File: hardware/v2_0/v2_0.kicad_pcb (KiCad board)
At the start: 2 copper layers, 90 parts, among them J1 USB_B_Mini, J11 NRFSWDCLK, J12 NRFSWDIO, J13 GND, J14 NRFGPIO, J15 USB_B_Mini, J16 DRV1_MTR2, J18 USB_A, J19 Conn_01x02_Male, J2 CAN, J3 PWR, J4 Power_terminal, J5 DRV1_MTR1, J6 DRV1_MTR2, J7 Conn_01x02_Male, J8 DRV1_MTR1, J9 UART, P1 SWD, Q1 Q_NMOS_GSD, Q2 Q_NMOS_GSD, U1 TJA1051TK-3, U10 DRV8848, U2 STM32F40X_LQFP64, U3 BMI160, U4 MCP16311/2, U5 DRV8848, U8 BMD-340-A-R, U9 ADP2303ARDZ-5.0, Y1 8M

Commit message: I hope it is time for routing soon
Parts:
- added J10: SERV1, Connector_PinHeader_2.54mm:PinHeader_1x03_P2.54mm_Vertical, F.Cu at (142.5, 71.0)
- added P2: SWD, Connector_JST:JST_PH_B6B-PH-K_1x06_P2.00mm_Vertical, F.Cu at (171.0, 104.3)
- added R19: 220R, Resistor_SMD:R_0603_1608Metric, F.Cu at (132.7, 96.0)
- added R20: 220R, Resistor_SMD:R_0603_1608Metric, F.Cu at (145.3, 82.2)
- added R21: 22R, Resistor_SMD:R_0603_1608Metric_Pad1.05x0.95mm_HandSolder, F.Cu at (150.2, 121.5)
- added R22: 22R, Resistor_SMD:R_0603_1608Metric_Pad1.05x0.95mm_HandSolder, F.Cu at (154.6, 121.5)
- J11: value NRFSWDCLK -> SERV2; footprint TestPoint:TestPoint_Pad_1.5x1.5mm -> Connector_PinHeader_2.54mm:PinHeader_1x03_P2.54mm_Vertical
- J12: value NRFSWDIO -> SPI; footprint TestPoint:TestPoint_Pad_1.5x1.5mm -> Connector_JST:JST_PH_B6B-PH-K_1x06_P2.00mm_Vertical
- J13: value GND -> UART5; footprint TestPoint:TestPoint_Pad_1.5x1.5mm -> Connector_JST:JST_PH_B4B-PH-K_1x04_P2.00mm_Vertical
- J9: value UART -> USART4_UART4
- moved J12 68.4 mm to (100.8, 78.0)
- moved C23 53.4 mm to (130.0, 120.9)
- moved R8 49.6 mm to (103.8, 126.8)
- moved R6 48.9 mm to (99.8, 126.8)
- moved R2 48.8 mm to (146.8, 75.0)
- moved C17 48.1 mm to (122.7, 125.4)
- moved R12 46.9 mm to (134.0, 120.1)
- moved C7 44.8 mm to (146.8, 72.5)
- moved R5 43.8 mm to (144.7, 84.7)
- moved U2 43.0 mm to (121.0, 76.0)
- moved R10 42.0 mm to (196.1, 74.5)
- moved C19 41.4 mm to (142.9, 110.7)
- moved J13 41.2 mm to (125.7, 85.9)
- moved C21 41.1 mm to (130.0, 118.3)
- moved R3 40.9 mm to (140.8, 88.7)
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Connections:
- net Net-(U2-Pad53) renamed /base_sheet/UART5_TX
- net Net-(U2-Pad54) renamed /base_sheet/UART5_RX
- J11 pad 1: NRFSWDCLK -> Net-(J11-Pad1)
- J12 pad 1: NRFSWDIO -> /base_sheet/SPI2_MOSI
- J15 pad 2: NRFUSBD- -> Net-(J15-Pad2)
- J15 pad 3: NRFUSBD+ -> Net-(J15-Pad3)
- U2 pad 10: Net-(U2-Pad10) -> NRFSWDCLK
- U2 pad 29: Net-(U2-Pad29) -> /base_sheet/SERV1
- U2 pad 30: Net-(U2-Pad30) -> /base_sheet/SERV2
- U2 pad 33: Net-(U2-Pad33) -> /base_sheet/SPI2_NSS
- U2 pad 34: Net-(U2-Pad34) -> /base_sheet/SPI2_SCK
- U2 pad 35: NRFSWDIO -> /base_sheet/SPI2_MISO
- U2 pad 36: NRFSWDCLK -> /base_sheet/SPI2_MOSI
- U2 pad 9: Net-(U2-Pad9) -> NRFSWDIO

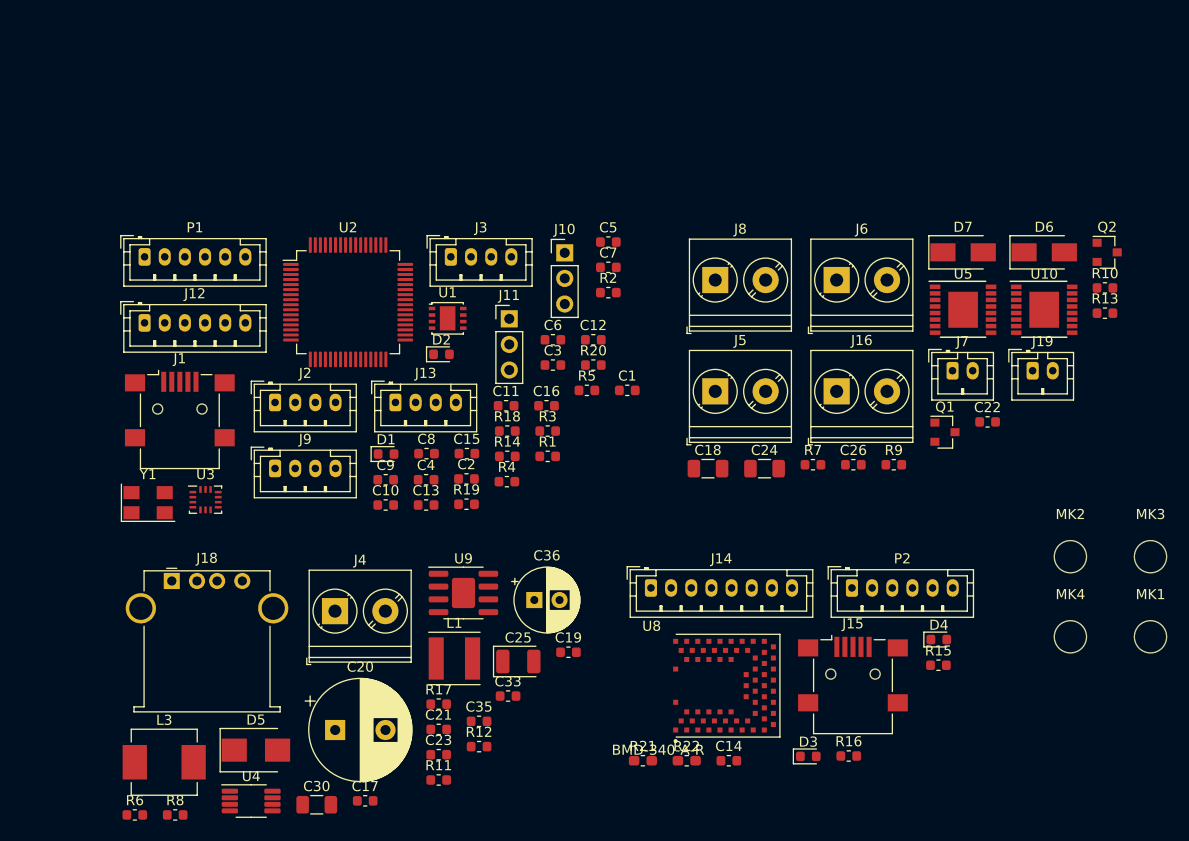
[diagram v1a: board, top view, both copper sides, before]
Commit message: adding an audio jack!
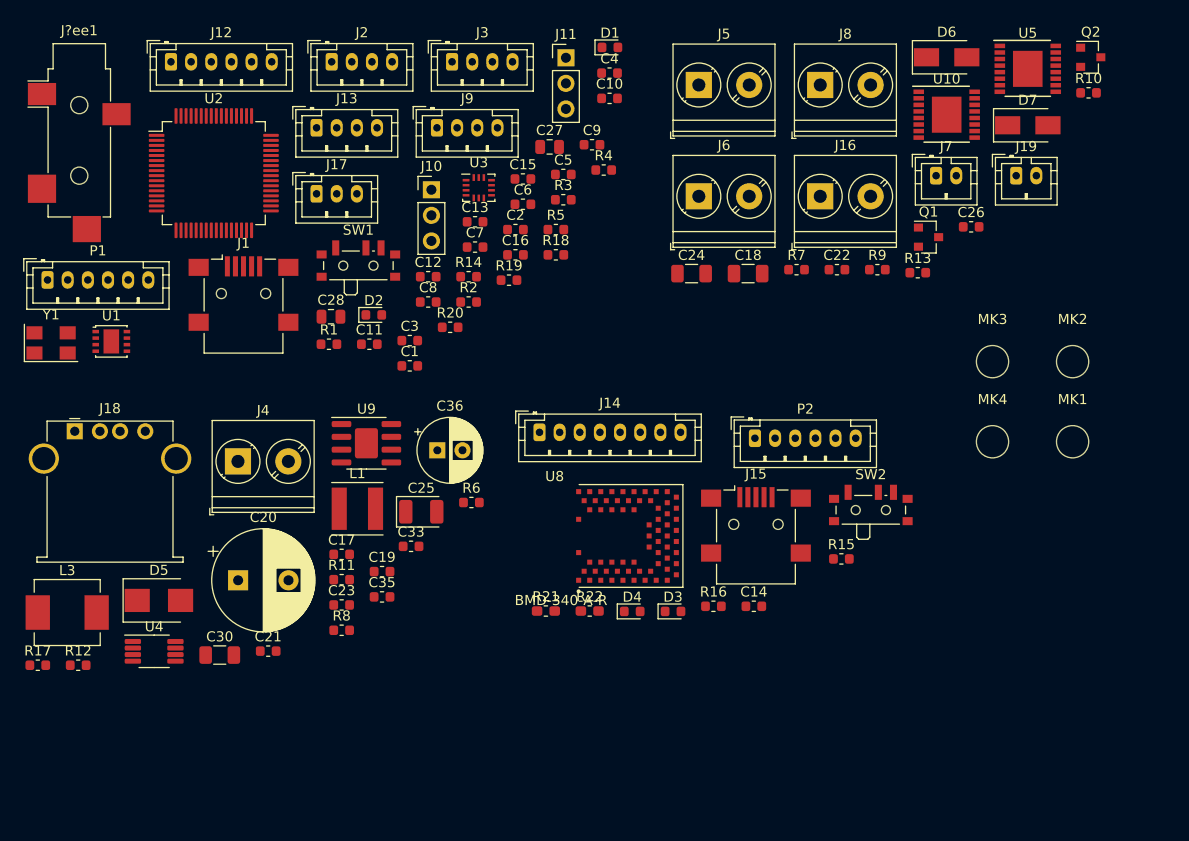
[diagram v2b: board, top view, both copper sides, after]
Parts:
- added C27: 10uF, Capacitor_SMD:C_0805_2012Metric, F.Cu at (141.0, 60.5)
- added C28: 10uF, Capacitor_SMD:C_0805_2012Metric, F.Cu at (119.3, 77.4)
- added J17: Conn_01x03_Male, Connector_JST:JST_PH_B3B-PH-K_1x03_P2.00mm_Vertical, F.Cu at (117.9, 65.2)
- added J?ee1: AudioJack3_Ground, Connector_Audio:Jack_3.5mm_CUI_SJ-3524-SMT_Horizontal, F.Cu at (94.3, 58.9)
- added SW1: MCU_USB_POWER, Button_Switch_SMD:SW_SPDT_PCM12, F.Cu at (122.0, 72.0)
- added SW2: NRF_USB_POWER, Button_Switch_SMD:SW_SPDT_PCM12, F.Cu at (172.9, 96.2)
- J19: value Conn_01x02_Male -> MTR1_CON
- J7: value Conn_01x02_Male -> MTR2_CON
- R14, R18: value R_Small -> 22R
- moved C10 46.1 mm to (146.9, 55.7)
- moved D1 46.1 mm to (147.0, 50.7)
- moved R6 45.6 mm to (133.2, 95.8)
- moved C4 44.3 mm to (146.9, 53.2)
- moved U3 41.2 mm to (134.0, 64.6)
- moved R12 40.6 mm to (94.2, 112.0)
- moved R17 40.0 mm to (90.2, 112.0)
- moved C9 39.1 mm to (145.2, 60.3)
- moved J9 37.4 mm to (129.8, 58.6)
- moved J2 34.3 mm to (119.4, 52.1)
- moved U1 33.5 mm to (97.5, 79.8)
- moved R4 32.4 mm to (146.4, 62.8)
- moved D4 30.6 mm to (149.2, 106.6)
- moved J5 30.5 mm to (155.8, 54.4)
- moved C13 28.5 mm to (133.6, 68.0)
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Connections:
- J1 pad 1: +5V -> Net-(J1-Pad1)
- J15 pad 1: +5V -> Net-(J15-Pad1)

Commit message: tweaks
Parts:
- added C29: 100uF, Capacitor_THT:CP_Radial_D10.0mm_P5.00mm, F.Cu at (114.9, 106.0)
- added C31: 100uF, Capacitor_THT:CP_Radial_D10.0mm_P5.00mm, F.Cu at (114.9, 117.5)
- added SW3: BOOT0, Button_Switch_SMD:SW_SPDT_PCM12, F.Cu at (118.9, 78.2)
- D6, D7: footprint Diode_SMD:D_SMA -> Diode_SMD:D_SMB
- J17: value Conn_01x03_Male -> DAC
- P2: value SWD -> NRFSWD
- moved D6 115.3 mm to (91.5, 125.1)
- moved R17 114.9 mm to (197.6, 71.3)
- moved R10 114.5 mm to (106.0, 127.8)
- moved Q2 111.1 mm to (111.8, 125.6)
- moved D7 110.9 mm to (99.8, 125.1)
- moved J8 98.8 mm to (90.8, 116.3)
- moved R12 94.8 mm to (184.7, 84.0)
- moved C26 88.8 mm to (116.1, 127.1)
- moved J19 85.4 mm to (126.2, 123.0)
- moved J5 82.5 mm to (90.8, 105.2)
- moved U5 79.6 mm to (127.2, 103.6)
- moved C21 78.4 mm to (184.7, 78.9)
- moved R13 77.2 mm to (120.1, 124.6)
- moved J16 76.2 mm to (102.9, 105.2)
- moved J7 75.1 mm to (126.2, 116.4)
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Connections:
- U2 pad 28: Net-(U2-Pad28) -> GND
- U2 pad 60: GND -> /base_sheet/BOOT0
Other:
- copper layers 2 -> 4
- rule pad_to_mask_clearance: 0.051 -> 0.01
- rule solder_mask_min_width: 0.25 -> 0.025
- rule trace_min: 0.2 -> 0.18
- rule via_min_size: 0.4 -> 0.3

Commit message: small tweaks
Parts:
- added C32: 47uF, Capacitor_THT:CP_Radial_D6.3mm_P2.50mm, F.Cu at (174.4, 48.1)
- J?ee1: footprint Connector_Audio:Jack_3.5mm_CUI_SJ-3524-SMT_Horizontal -> v2_0:Jack_3.5mm_CUI_SJ-3524-SMT_Horizontal
- U8: footprint crf1:RIGADO_BMD-340-A-R -> v2_0:RIGADO_BMD-340-A-R
- moved Q1 41.3 mm to (92.3, 107.6)
- moved C13 38.4 mm to (98.6, 77.2)
- moved J4 38.0 mm to (136.5, 65.3)
- moved Q2 37.9 mm to (113.9, 87.8)
- moved R7 36.8 mm to (96.5, 109.1)
- moved R13 36.7 mm to (86.4, 109.9)
- moved C36 36.5 mm to (157.7, 65.2)
- moved J16 36.4 mm to (71.2, 87.2)
- moved C26 35.8 mm to (113.7, 91.3)
- moved C31 35.4 mm to (95.4, 88.0)
- moved R12 35.2 mm to (152.7, 69.4)
- moved C20 35.0 mm to (154.9, 50.0)
- moved J6 35.0 mm to (83.3, 87.2)
- moved C8 33.8 mm to (122.3, 58.1)
- moved C7 33.3 mm to (113.1, 65.4)
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
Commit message: tweaks prepare for routing
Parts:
- moved SW2 43.0 mm to (182.2, 126.6)
- moved J?ee1 38.8 mm to (100.6, 79.3)
- moved C10 37.0 mm to (139.2, 93.9)
- moved C18 37.0 mm to (141.2, 109.5)
- moved C5 37.0 mm to (149.5, 80.8)
- moved D2 37.0 mm to (153.2, 75.7)
- moved C13 37.0 mm to (125.3, 102.8)
- moved C17 37.0 mm to (199.6, 88.3)
- moved C21 37.0 mm to (198.6, 83.3)
- moved C22 37.0 mm to (127.2, 132.2)
- moved C23 37.0 mm to (191.6, 91.1)
- moved C24 37.0 mm to (113.9, 132.6)
- moved C26 37.0 mm to (140.4, 116.9)
- moved C27 37.0 mm to (145.2, 81.0)
- moved C31 37.0 mm to (122.1, 113.6)
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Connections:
- C29 pad 1: VIN -> V_IN
- C31 pad 1: VIN -> V_IN

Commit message: fixed mistake in schematics
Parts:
- J9: value USART4_UART4 -> USART3_UART4
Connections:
- J13 pad 2: UART_RXD -> /base_sheet/UART5_RX
- J13 pad 3: UART_TXD -> /base_sheet/UART5_TX

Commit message: started routing
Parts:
- moved J3 117.1 mm to (240.2, 94.2), turned to -90 degrees
- moved J4 80.9 mm to (237.0, 57.6), turned to 90 degrees
- moved J10 71.6 mm to (206.0, 72.6), turned to 90 degrees
- moved R12 69.5 mm to (229.6, 47.0), turned to -90 degrees
- moved J18 64.7 mm to (229.0, 83.6), turned to 90 degrees
- moved C30 60.6 mm to (221.8, 57.4), turned to 90 degrees
- moved J11 57.2 mm to (206.0, 69.0), turned to 90 degrees
- moved C33 56.7 mm to (231.2, 47.0), turned to 90 degrees
- moved C14 56.1 mm to (218.0, 152.8)
- moved D3 56.1 mm to (209.9, 153.3)
- moved D4 56.1 mm to (214.0, 153.3)
- moved J14 56.1 mm to (202.1, 136.1)
- moved J15 56.1 mm to (222.2, 144.7)
- moved P2 56.1 mm to (222.1, 136.1)
- moved R15 56.1 mm to (222.0, 152.8)
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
